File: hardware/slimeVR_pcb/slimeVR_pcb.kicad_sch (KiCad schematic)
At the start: 60 parts, among them J1 HRO_TYPE-C-31-M-12, J3 Conn_ARM_JTAG_SWD_10, Q1 8205A, SW1 SK12D07VG4, SW2 SW_Push, U1 ESP32-S2-WROVER, U10 AP2112K-3.3, U2 TP4057, U3 ICM-45686, U5 QMC6309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

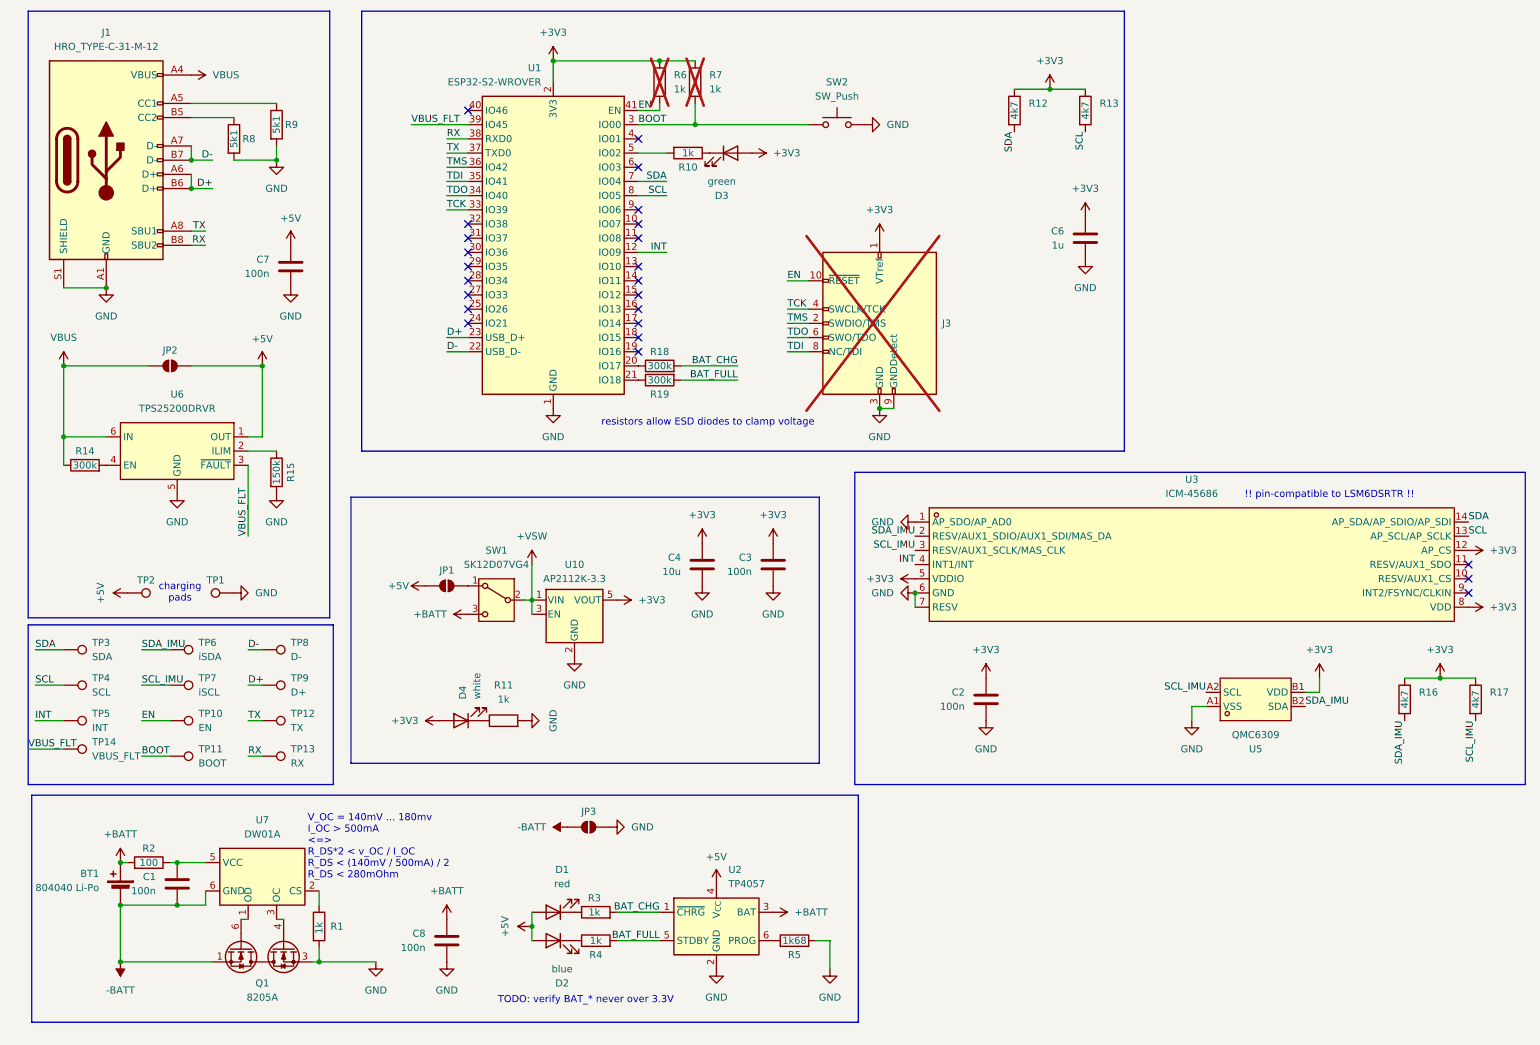
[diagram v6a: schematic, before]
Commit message: allow ESP to read/write CC pins for future use
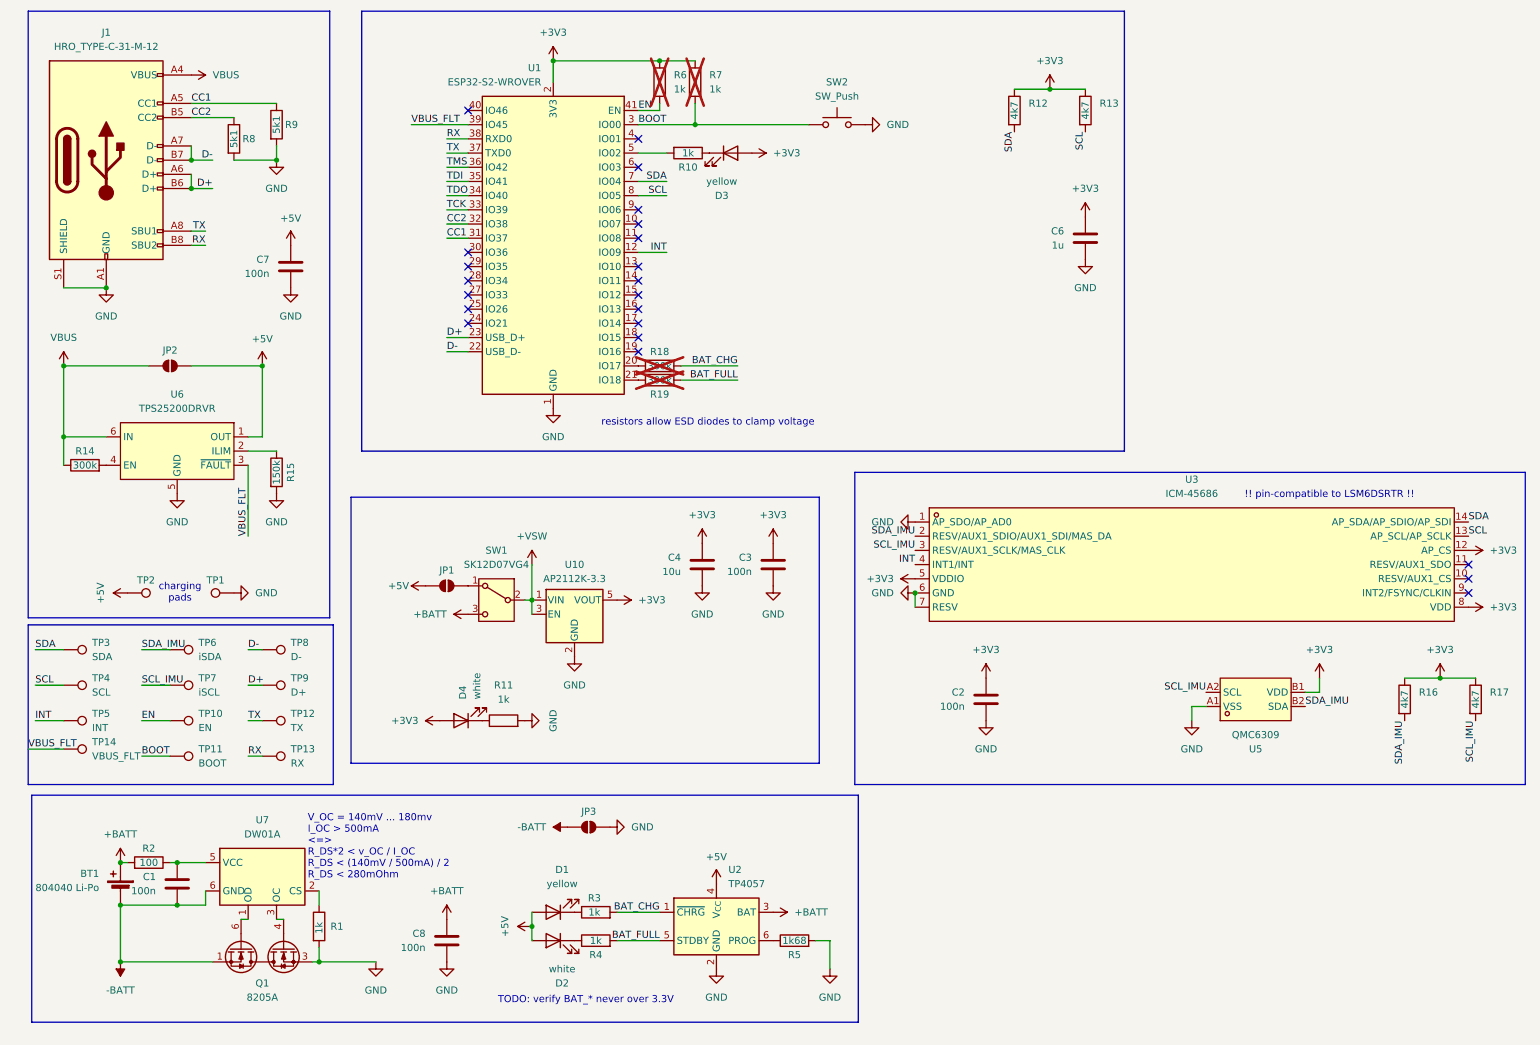
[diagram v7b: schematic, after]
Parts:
- removed J3: Conn_ARM_JTAG_SWD_10, Connector:Tag-Connect_TC2050-IDC-NL_2x05_P1.27mm_Vertical, symbol Connector:Conn_ARM_JTAG_SWD_10
- BT1: now in the parts list
- D1: value red -> yellow; LCSC C2286 -> C2296; LCSC Part C2286 -> (none)
- D2: value blue -> white; LCSC C2288 -> C34499; LCSC Part C2288 -> (none)
- D3: value green -> yellow; LCSC C2289 -> C2296; LCSC Part C2289 -> (none)
- R18, R19: now not fitted; now left out of the parts list
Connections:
- net CC1: now reaches U1.31 (IO37)
- net CC1: now also J1.A5 (CC1), R9.1
- net CC2: now reaches U1.32 (IO38)
- net CC2: now also J1.B5 (CC2), R8.1
- no-connect marks 24 -> 22

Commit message: tried to use an FUSB302 to supply vconn
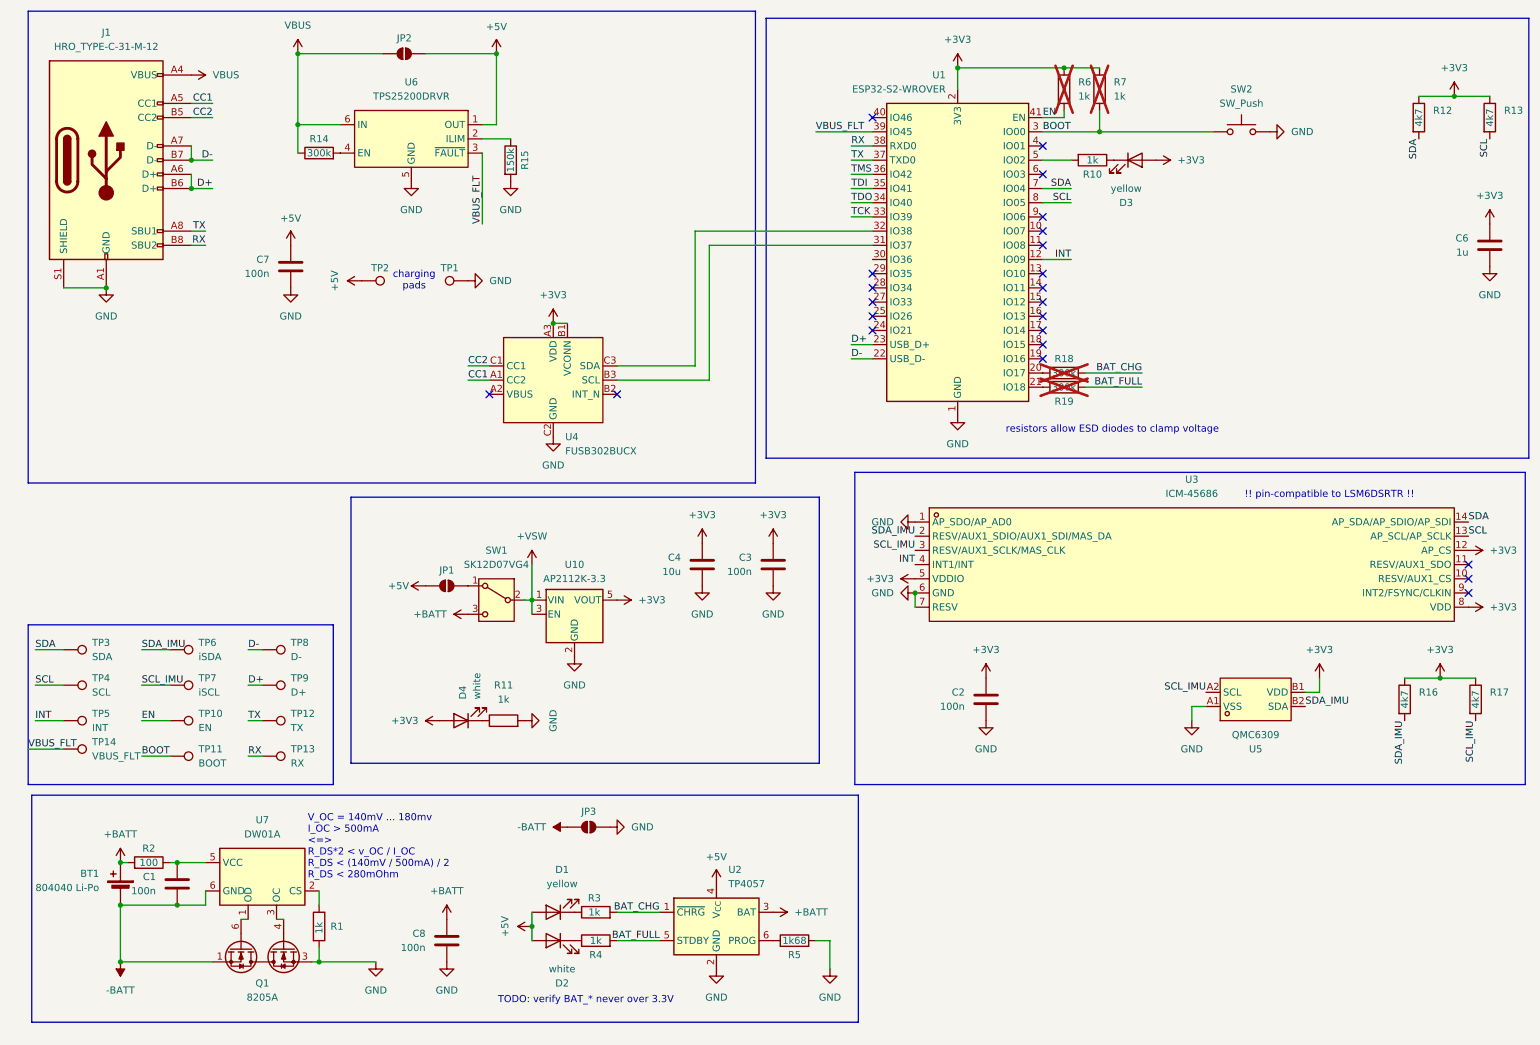
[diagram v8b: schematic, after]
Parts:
- removed R8, R9: 5k1, Resistor_SMD:R_0603_1608Metric_Pad0.98x0.95mm_HandSolder, symbol Device:R
- added U4: FUSB302BUCX, easyeda2kicad:WLCSP-9_L1.3-W1.2-R3-C3-P0.40-TL, symbol slime_parts:FUSB302BUCX
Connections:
- net +3V3: now also U4.A3 (VDD), U4.B1 (VCONN)
- net CC1: now also U4.A1 (CC2); no longer U1.31 (IO37)
- net CC2: now also U4.C1 (CC1); no longer U1.32 (IO38)
- net GND: now also U4.C2 (GND)
- new net: U1.31 (IO37), U4.B3 (SCL)
- new net: U1.32 (IO38), U4.C3 (SDA)
- no-connect marks 22 -> 23
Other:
- moved on the sheet: C6, D3, JP2, R10, R12, R13, R14, R15, R18, R19, R6, R7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
